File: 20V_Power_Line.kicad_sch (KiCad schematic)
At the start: 26 parts, among them Q5 CSD18543Q3A, Q6 CSD18543Q3A, U7 LM25145RGYR

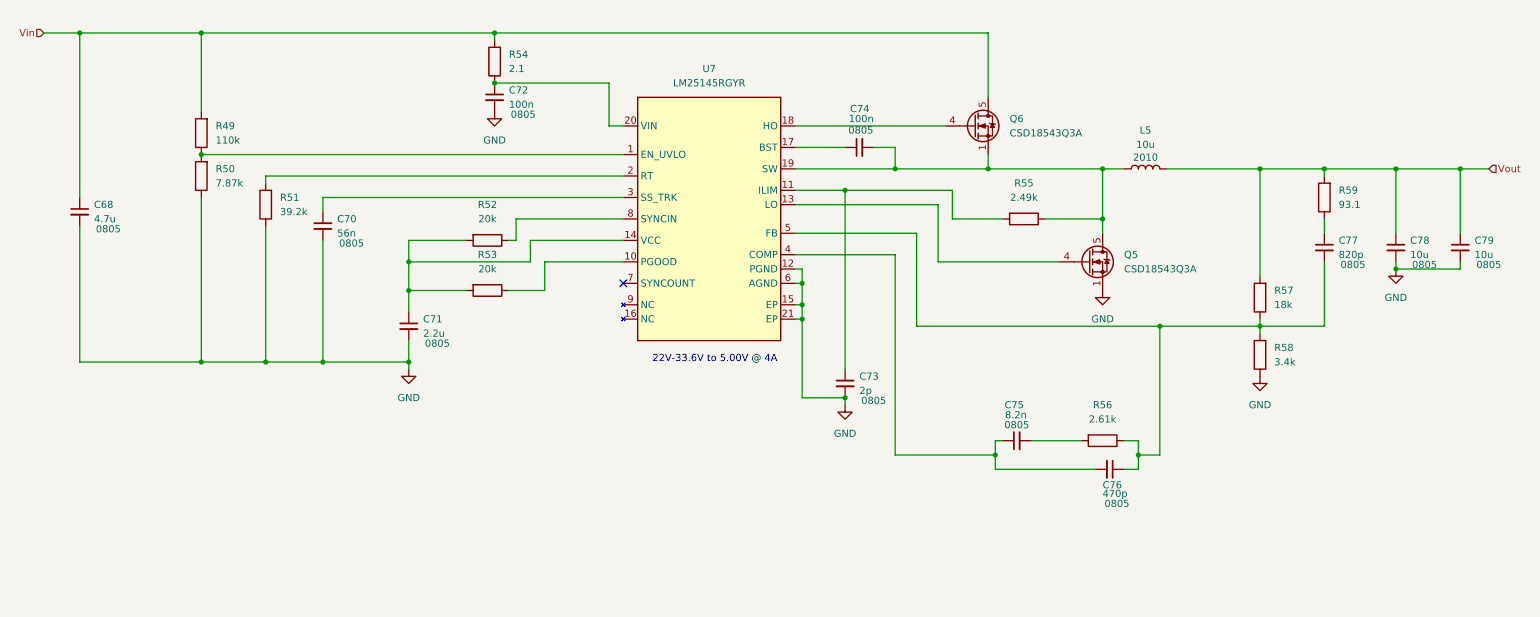
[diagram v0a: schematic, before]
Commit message: added more power lines
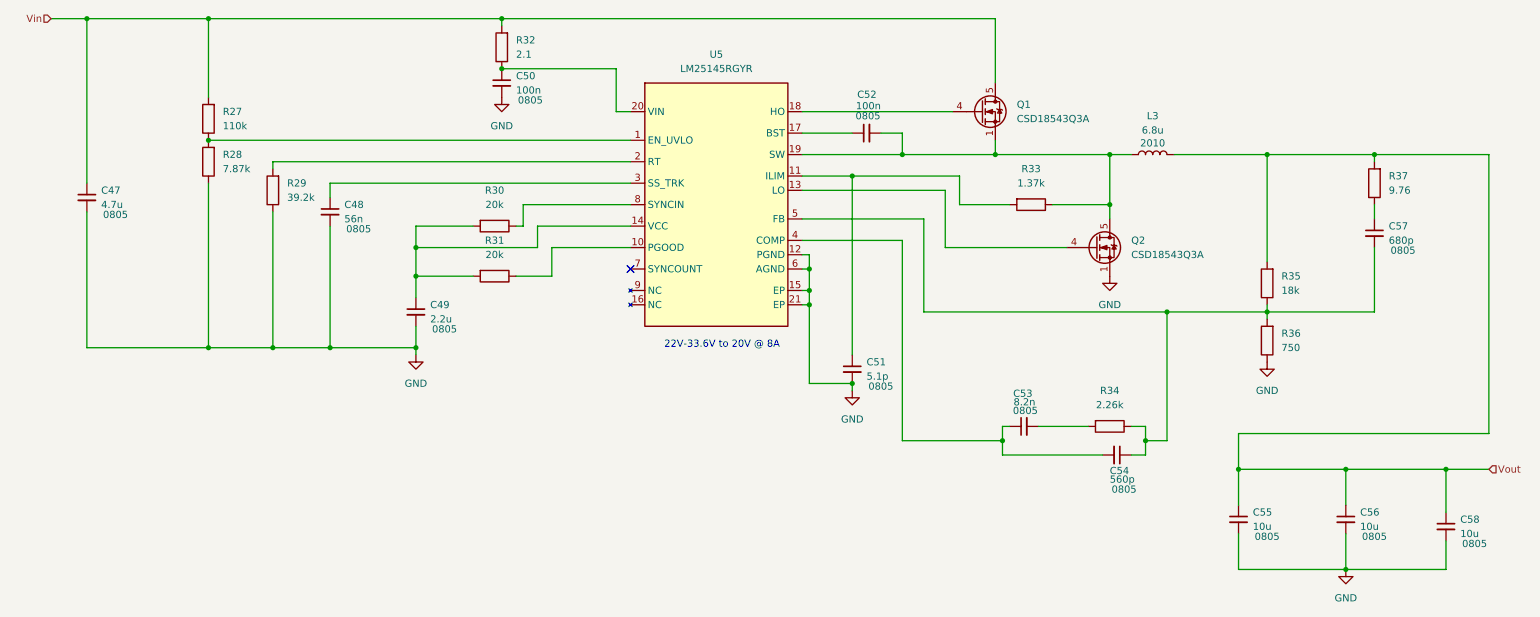
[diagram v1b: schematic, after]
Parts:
- removed C68: 4.7u, Capacitor_SMD:C_0805_2012Metric_Pad1.18x1.45mm_HandSolder, symbol Device:C_Small
- removed C70: 56n, Capacitor_SMD:C_0805_2012Metric_Pad1.18x1.45mm_HandSolder, symbol Device:C_Small
- removed C71: 2.2u, Capacitor_SMD:C_0805_2012Metric_Pad1.18x1.45mm_HandSolder, symbol Device:C_Small
- removed C72, C74: 100n, Capacitor_SMD:C_0805_2012Metric_Pad1.18x1.45mm_HandSolder, symbol Device:C_Small
- removed C73: 2p, Capacitor_SMD:C_0805_2012Metric_Pad1.18x1.45mm_HandSolder, symbol Device:C_Small
- removed C75: 8.2n, Capacitor_SMD:C_0805_2012Metric_Pad1.18x1.45mm_HandSolder, symbol Device:C_Small
- removed C76: 470p, Capacitor_SMD:C_0805_2012Metric_Pad1.18x1.45mm_HandSolder, symbol Device:C_Small
- removed C77: 820p, Capacitor_SMD:C_0805_2012Metric_Pad1.18x1.45mm_HandSolder, symbol Device:C_Small
- removed C78, C79: 10u, Capacitor_SMD:C_0805_2012Metric_Pad1.18x1.45mm_HandSolder, symbol Device:C_Small
- removed L5: 10u, Inductor_SMD_Wurth:L_Wurth_WE-LQSH-2010, symbol Device:L
- removed Q5, Q6: CSD18543Q3A, Package_SON:VSON-8_3.3x3.3mm_P0.65mm_NexFET, symbol Transistor_FET:CSD18543Q3A
- removed R49, R50, R51, R52, R53, R54, R55, R56, R57, R58, R59: 150K_0603, PCM_4ms_Resistor:R_0805_2012Metric, symbol PCM_4ms_Resistor:150K_0603
- removed U7: LM25145RGYR, Project_Star_Regulator_Switching:RGY0020B, symbol Project_Star_Regulator_Switching:LM25145
- added C47: 4.7u, Capacitor_SMD:C_0805_2012Metric_Pad1.18x1.45mm_HandSolder, symbol Device:C_Small
- added C48: 56n, Capacitor_SMD:C_0805_2012Metric_Pad1.18x1.45mm_HandSolder, symbol Device:C_Small
- added C49: 2.2u, Capacitor_SMD:C_0805_2012Metric_Pad1.18x1.45mm_HandSolder, symbol Device:C_Small
- added C50, C52: 100n, Capacitor_SMD:C_0805_2012Metric_Pad1.18x1.45mm_HandSolder, symbol Device:C_Small
- added C51: 5.1p, Capacitor_SMD:C_0805_2012Metric_Pad1.18x1.45mm_HandSolder, symbol Device:C_Small
- added C53: 8.2n, Capacitor_SMD:C_0805_2012Metric_Pad1.18x1.45mm_HandSolder, symbol Device:C_Small
- added C54: 560p, Capacitor_SMD:C_0805_2012Metric_Pad1.18x1.45mm_HandSolder, symbol Device:C_Small
- added C55, C56, C58: 10u, Capacitor_SMD:C_0805_2012Metric_Pad1.18x1.45mm_HandSolder, symbol Device:C_Small
- added C57: 680p, Capacitor_SMD:C_0805_2012Metric_Pad1.18x1.45mm_HandSolder, symbol Device:C_Small
- added L3: 6.8u, Inductor_SMD_Wurth:L_Wurth_WE-LQSH-2010, symbol Device:L
- added Q1, Q2: CSD18543Q3A, Package_SON:VSON-8_3.3x3.3mm_P0.65mm_NexFET, symbol Transistor_FET:CSD18543Q3A
- added R27, R28, R29, R30, R31, R32, R33, R34, R35, R36, R37: 150K_0603, PCM_4ms_Resistor:R_0805_2012Metric, symbol PCM_4ms_Resistor:150K_0603
- added U5: LM25145RGYR, Project_Star_Regulator_Switching:RGY0020B, symbol Project_Star_Regulator_Switching:LM25145
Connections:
- net GND: now also C47.2, C48.2, C49.2, C50.2, C51.2, C55.2, C56.2, C58.2, Q2.1 (S), Q2.2 (S), Q2.3 (S), R28.1, R29.1, R36.1, U5.12 (PGND), U5.15 (EP), U5.21 (EP), U5.6 (AGND)
- net Vin: now also C47.1, Q1.5 (D), R27.2, R32.2
- net Vout: now also C55.1, C56.1, C58.1, L3.2, R35.2, R37.2
- new net: R27.1, R28.2, U5.1 (EN_UVLO)
- new net: C52.2, L3.1, Q1.1 (S), Q1.2 (S), Q1.3 (S), Q2.5 (D), R33.1, U5.19 (SW)
- new net: C51.1, R33.2, U5.11 (ILIM)
- new net: C54.1, C57.2, R34.1, R35.1, R36.2, U5.5 (FB)
- new net: C50.1, R32.1, U5.20 (VIN)
- new net: R31.1, U5.10 (PGOOD)
- new net: Q2.4 (G), U5.13 (LO)
- new net: C49.1, R30.2, R31.2, U5.14 (VCC)
- new net: C52.1, U5.17 (BST)
- new net: Q1.4 (G), U5.18 (HO)
- new net: R29.2, U5.2 (RT)
- new net: C48.1, U5.3 (SS_TRK)
- new net: C53.1, C54.2, U5.4 (COMP)
- new net: R30.1, U5.8 (SYNCIN)
- new net: C57.1, R37.1
- new net: C53.2, R34.2
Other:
- note added: "22V-33.6V to 20V @ 8A"
- note removed: "22V-33.6V to 5.00V @ 4A"

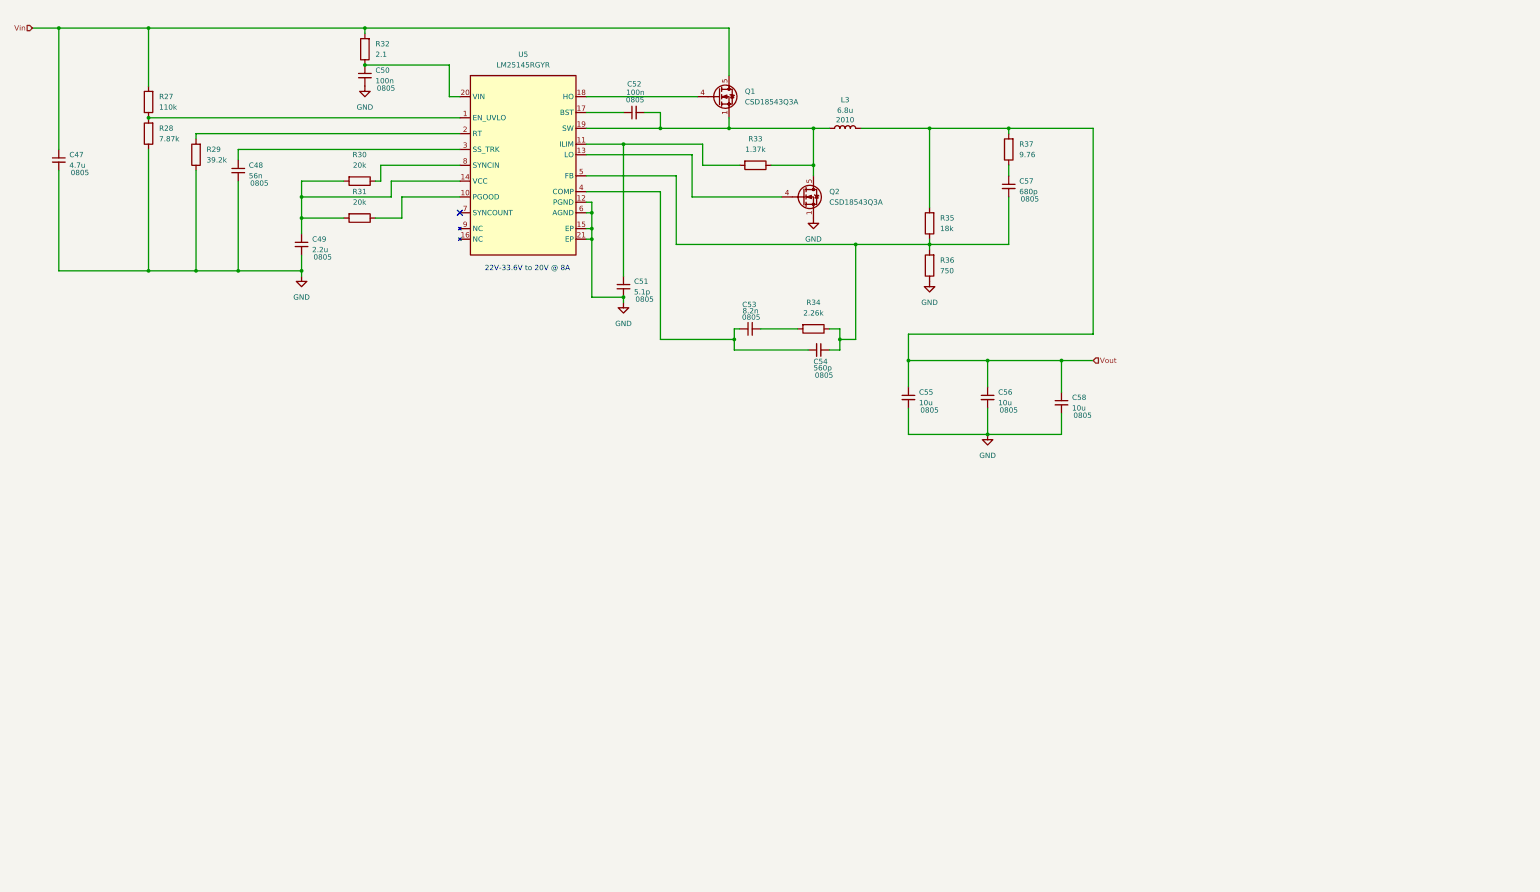
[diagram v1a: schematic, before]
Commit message: 20V line PCB v1
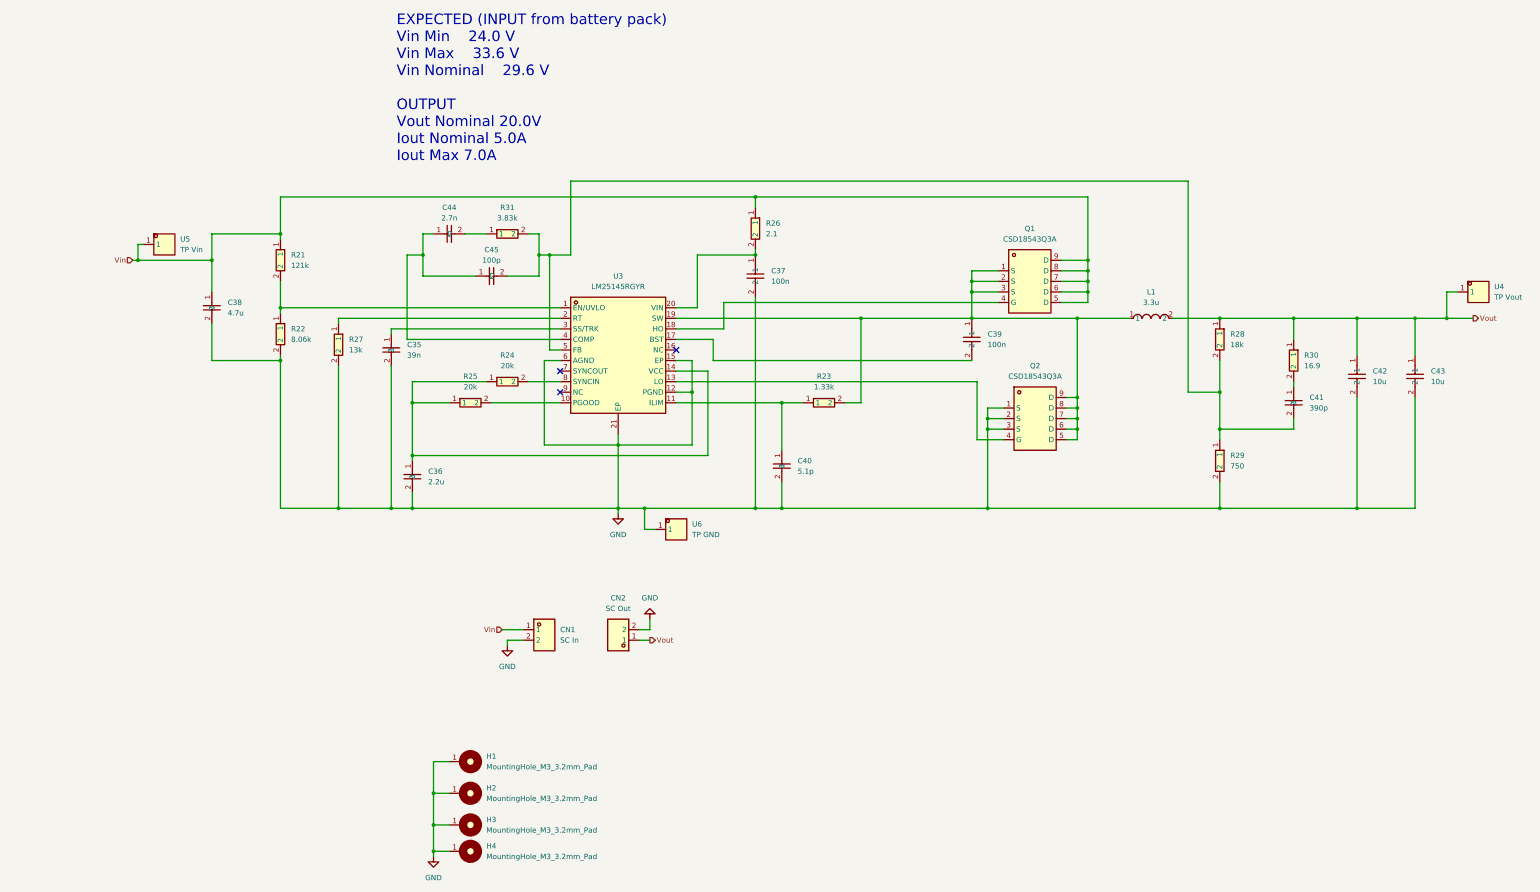
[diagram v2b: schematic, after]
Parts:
- removed C47: 4.7u, Capacitor_SMD:C_0805_2012Metric_Pad1.18x1.45mm_HandSolder, symbol Device:C_Small
- removed C48: 56n, Capacitor_SMD:C_0805_2012Metric_Pad1.18x1.45mm_HandSolder, symbol Device:C_Small
- removed C49: 2.2u, Capacitor_SMD:C_0805_2012Metric_Pad1.18x1.45mm_HandSolder, symbol Device:C_Small
- removed C50, C52: 100n, Capacitor_SMD:C_0805_2012Metric_Pad1.18x1.45mm_HandSolder, symbol Device:C_Small
- removed C51: 5.1p, Capacitor_SMD:C_0805_2012Metric_Pad1.18x1.45mm_HandSolder, symbol Device:C_Small
- removed C53: 8.2n, Capacitor_SMD:C_0805_2012Metric_Pad1.18x1.45mm_HandSolder, symbol Device:C_Small
- removed C54: 560p, Capacitor_SMD:C_0805_2012Metric_Pad1.18x1.45mm_HandSolder, symbol Device:C_Small
- removed C55, C56, C58: 10u, Capacitor_SMD:C_0805_2012Metric_Pad1.18x1.45mm_HandSolder, symbol Device:C_Small
- removed C57: 680p, Capacitor_SMD:C_0805_2012Metric_Pad1.18x1.45mm_HandSolder, symbol Device:C_Small
- removed L3: 6.8u, Inductor_SMD_Wurth:L_Wurth_WE-LQSH-2010, symbol Device:L
- removed Q1, Q2: CSD18543Q3A, Package_SON:VSON-8_3.3x3.3mm_P0.65mm_NexFET, symbol Transistor_FET:CSD18543Q3A
- removed R27, R28, R29, R30, R31, R32, R33, R34, R35, R36, R37: 150K_0603, PCM_4ms_Resistor:R_0805_2012Metric, symbol PCM_4ms_Resistor:150K_0603
- removed U5: LM25145RGYR, Project_Star_Regulator_Switching:RGY0020B, symbol Project_Star_Regulator_Switching:LM25145
- added C35: 39n, easyeda2kicad:C0603, symbol easyeda2kicad:0603B393K500NT
- added C36: 2.2u, easyeda2kicad:C1206, symbol easyeda2kicad:CL31B225KBHNNNE
- added C37, C39: 100n, easyeda2kicad:C0603, symbol easyeda2kicad:CC0603KRX7R9BB104
- added C38: 4.7u, easyeda2kicad:C1206, symbol easyeda2kicad:1206B475K500NT
- added C40: 5.1p, easyeda2kicad:C0402, symbol easyeda2kicad:0402CG5R1C500NT
- added C41: 390p, easyeda2kicad:C0603, symbol easyeda2kicad:0603B391K500NT
- added C42, C43: 10u, easyeda2kicad:C0805, symbol easyeda2kicad:GRM21BR61H106KE43L
- added C44: 2.7n, easyeda2kicad:C0603, symbol easyeda2kicad:0603B272K500NT
- added C45: 100p, easyeda2kicad:C0402, symbol easyeda2kicad:0402CG101J500NT
- added CN1: SC In, easyeda2kicad:CONN-TH_2P-P5.08_DIBO_DB128V-5.08, symbol easyeda2kicad:DB128V-5.08-2P-GN-S
- added CN2: SC Out, easyeda2kicad:CONN-TH_2P-P5.08_DIBO_DB128V-5.08, symbol easyeda2kicad:DB128V-5.08-2P-GN-S
- added H1, H2, H3, H4: MountingHole_M3_3.2mm_Pad, PCM_SL_Mechanical:MountingHole_3.2mm_Pad, symbol PCM_SL_Mechanical:MountingHole_M3_3.2mm_Pad
- added L1: 3.3u, easyeda2kicad:IND-SMD_L11.5-W10.0_SMMS1040, symbol easyeda2kicad:SMMS1040-3R3M
- added Q1, Q2: CSD18543Q3A, easyeda2kicad:VSONP-8_L3.1-W3.1-P0.65-LS3.5-BL, symbol easyeda2kicad:CSD18543Q3A
- added R21: 121k, easyeda2kicad:R0402, symbol easyeda2kicad:0402WGF1213TCE
- added R22: 8.06k, easyeda2kicad:R0603, symbol easyeda2kicad:0603WAF8061T5E
- added R23: 1.33k, easyeda2kicad:R0603, symbol easyeda2kicad:RC0603FR-071K33L
- added R24, R25: 20k, easyeda2kicad:R0603, symbol easyeda2kicad:0603WAF2002T5E
- added R26: 2.1, easyeda2kicad:R0603, symbol easyeda2kicad:RS-03L2R10FT
- added R27: 13k, easyeda2kicad:R0603, symbol easyeda2kicad:0603WAF1302T5E
- added R28: 18k, easyeda2kicad:R0603, symbol easyeda2kicad:0603WAF1802T5E
- added R29: 750, easyeda2kicad:R0402, symbol easyeda2kicad:RC0402JR-07750RL
- added R30: 16.9, easyeda2kicad:R0402, symbol easyeda2kicad:0402WGF169JTCE
- added R31: 3.83k, easyeda2kicad:R0402, symbol easyeda2kicad:0402WGF3831TCE
- added U3: LM25145RGYR, easyeda2kicad:VQFN-20_L4.5-W3.5-P0.50-BL-EP, symbol easyeda2kicad:LM25145RGYR
- added U4: TP Vout, easyeda2kicad:TEST-TH_BD3.17-P1.87, symbol easyeda2kicad:5011
- added U5: TP Vin, easyeda2kicad:TEST-TH_BD3.17-P1.87, symbol easyeda2kicad:5011
- added U6: TP GND, easyeda2kicad:TEST-TH_BD3.17-P1.87, symbol easyeda2kicad:5011
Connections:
- net GND: now also C35.2, C36.2, C37.2, C38.2, C40.2, C42.2, C43.2, CN1.2, CN2.2, H1.1, H2.1, H3.1, H4.1, Q2.1 (S), Q2.2 (S), Q2.3 (S), R22.2, R27.2, R29.2, U3.12 (PGND), U3.15 (EP), U3.21 (EP), U3.6 (AGND), U6.1
- net Vin: now also C38.1, CN1.1, Q1.5 (D), Q1.6 (D), Q1.7 (D), Q1.8 (D), Q1.9 (D), R21.1, R26.1, U5.1
- net Vout: now also C42.1, C43.1, CN2.1, L1.2, R28.1, R30.1, U4.1
- new net: R21.2, R22.1, U3.1 (EN/UVLO)
- new net: R25.2, U3.10 (PGOOD)
- new net: C40.1, R23.1, U3.11 (ILIM)
- new net: Q2.4 (G), U3.13 (LO)
- new net: C36.1, R24.1, R25.1, U3.14 (VCC)
- new net: C39.2, U3.17 (BST)
- new net: Q1.4 (G), U3.18 (HO)
- new net: C39.1, L1.1, Q1.1 (S), Q1.2 (S), Q1.3 (S), Q2.5 (D), Q2.6 (D), Q2.7 (D), Q2.8 (D), Q2.9 (D), R23.2, U3.19 (SW)
- new net: R27.1, U3.2 (RT)
- new net: C37.1, R26.2, U3.20 (VIN)
- new net: C35.1, U3.3 (SS/TRK)
- new net: C44.1, C45.1, U3.4 (COMP)
- new net: C41.2, C45.2, R28.2, R29.1, R31.2, U3.5 (FB)
- new net: R24.2, U3.8 (SYNCIN)
- new net: C41.1, R30.2
- new net: C44.2, R31.1
- no-connect marks 1 -> 3
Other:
- note added: "EXPECTED (INPUT from battery pack) Vin Min 24.0 V Vin Max 33.6 V Vin Nominal 29.6 V OUTPUT Vout Nominal 20.0V Iout Nominal 5.0A Iout Max 7.0A"
- note removed: "22V-33.6V to 20V @ 8A"

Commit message: 20V line V2
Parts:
- added Cin2: 4.7u, easyeda2kicad:C1206, symbol easyeda2kicad:1206B475K500NT
- added Cin3, Cout3, Cout4: 10u, easyeda2kicad:C0805, symbol easyeda2kicad:GRM21BR61H106KE43L
- renumbered C39 to Cbst1, C44 to Ccomp1, C45 to Ccomp2, C41 to Ccomp3, C40 to Cilim1, C38 to Cin1, C42 to Cout1, C43 to Cout2, C35 to Css1, C36 to Cvcc1, C37 to Cvin1, L1 to LF1, R31 to Rcomp1, R30 to Rcomp2, R29 to Rfbb1, R28 to Rfbt1, R23 to Rilim1, R25 to Rpgood1, R27 to Rt1, R21 to Ruv1, R22 to Ruv2, R24 to Rvcc1, R26 to Rvin1, U5 to U3, U3 to U4, U6 to U5, U4 to U6
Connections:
- net GND: now also Cin2.2, Cin3.2, Cout3.2, Cout4.2
- net Vin: now also Cin2.1, Cin3.1
- net Vout: now also Cout3.1, Cout4.1

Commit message: In Progress v3
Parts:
- removed LF1: 3.3u, easyeda2kicad:IND-SMD_L11.5-W10.0_SMMS1040, symbol easyeda2kicad:SMMS1040-3R3M
- added Csnub1: DNP, easyeda2kicad:C0402, symbol easyeda2kicad:0402CG5R1C500NT
- added LF1: 3.3u, easyeda2kicad:IND-SMD_L13.8-W12.8, symbol easyeda2kicad:CYA1250-3.3UH
- added Rbst1: 4.7, easyeda2kicad:R0805, symbol easyeda2kicad:0805W8F470KT5E
- added Rsnub1: DNP, easyeda2kicad:R0805, symbol easyeda2kicad:0805W8F470KT5E
- renumbered Rfbt1 to Rfb1, Rfbb1 to Rfb2, Rt1 to Rrt1
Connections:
- net GND: now also Csnub1.2
- net Vout: now also LF1.2
- net at U4.17 (BST): now also Rbst1.1; no longer Cbst1.2
- net at Cbst1.1, Q1.1 (S), Q1.2 (S)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: now also LF1.1, Rsnub1.2
- new net: Cbst1.2, Rbst1.2
- new net: Csnub1.1, Rsnub1.1
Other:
- moved on the sheet: Cbst1, Q2
